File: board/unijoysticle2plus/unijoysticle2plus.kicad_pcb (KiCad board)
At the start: 4 copper layers, 62 x 49 mm, 43 parts, among them J1 DB9_Female, J2 DB9_Female, J3 USB_B_Micro, Q1 S8050, Q2 S8050, SW1 RESET, SW2 JOY SWAP, U1 74HC05, U2 74HC05, U3 74HC05, U4 ESP32-WROOM-32D, U5 AMS1117-3.3, U6 CH340C

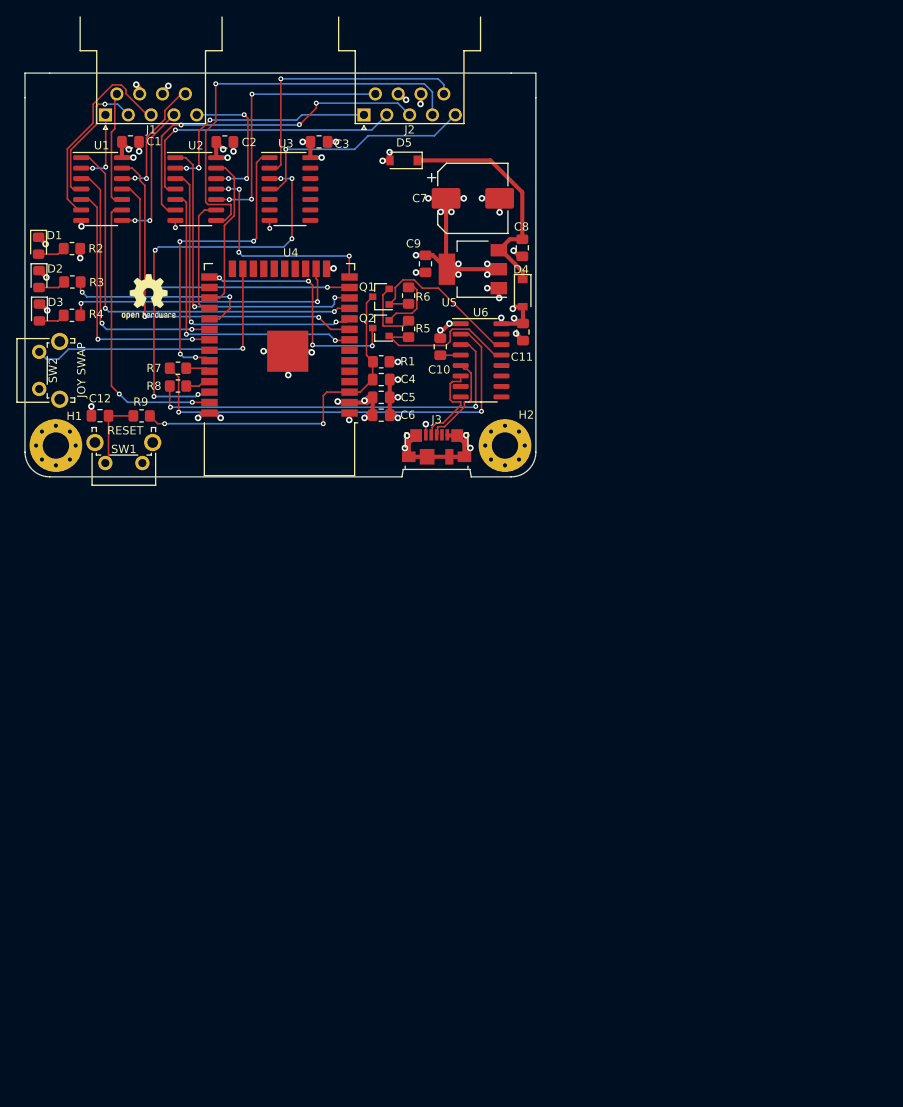
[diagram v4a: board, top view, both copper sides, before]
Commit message: unijoysticle2+: rev C WIP
- 5819 package: using SMA instead of SOD-123:
    - I thought the diode was fauly or something... so I dediced to
      change for another one. But I think the bug is somewhere else.
      In any case, using the new part (with different package)
- CH340C: powered using v3.3 instead of v5.
    - ESP EN should be high (v3.3) or low (0), but if CH340 is powered
      using v5, then DTR might have ~4V... instead of v3.3
- Using one MUN5214D insetad of two S8050 + resistors
    - less space, less routing, cheaper... although might not be as easy
      to solder as the S8050
- Using only one power place: removed VBUS and C64-5V power planes.
    - The only power plane is the v3.3+ one
- Layout changed a bit to based on the new components.
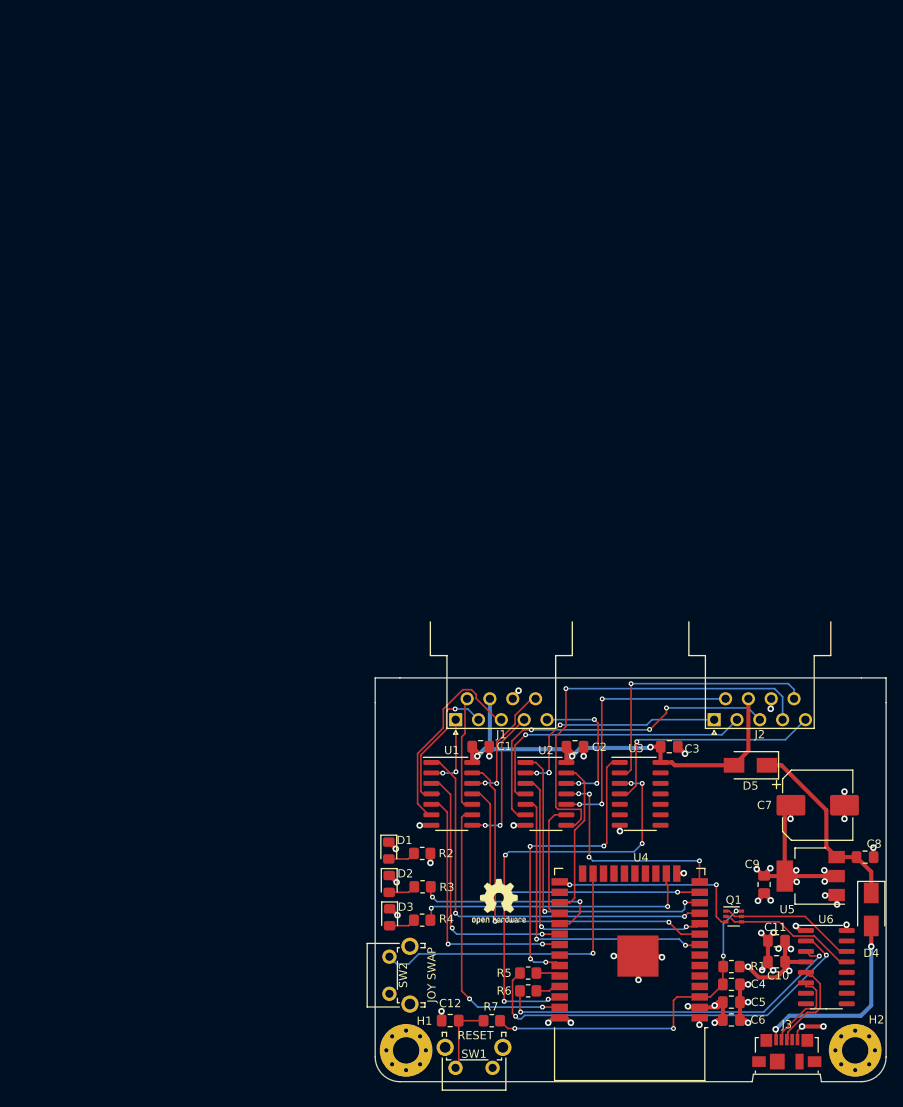
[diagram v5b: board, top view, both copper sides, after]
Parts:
- removed Q2: S8050, Package_TO_SOT_SMD:SOT-23
- removed the R5 at (86.8, 57.0)
- removed the R6 at (86.8, 52.9)
- C10: value .1uF -> 1uF
- D4, D5: footprint Diode_SMD:D_SOD-123 -> Diode_SMD:D_SMA
- Q1: value S8050 -> MUN5211DW1; footprint Package_TO_SOT_SMD:SOT-23 -> Package_TO_SOT_SMD:SOT-363_SC-70-6
- R2, R3, R4: value 300 -> 1k
- moved Q1 86.5 mm to (126.2, 128.3), turned to 0 degrees
- moved D4 85.9 mm to (142.9, 127.4)
- moved C9 85.8 mm to (129.9, 124.4)
- moved C10 85.1 mm to (131.4, 133.8), turned to 180 degrees
- moved C8 84.8 mm to (142.2, 121.1), turned to 0 degrees
- moved H2 84.8 mm to (141.0, 144.5)
- moved C1 84.8 mm to (95.5, 107.7)
- moved C2 84.8 mm to (107.0, 107.7)
- moved C3 84.8 mm to (118.4, 107.7)
- moved C4 84.8 mm to (126.0, 136.5)
- moved C6 84.8 mm to (126.0, 140.8)
- moved D1 84.8 mm to (84.4, 120.3)
- moved D2 84.8 mm to (84.4, 124.3)
- moved D3 84.8 mm to (84.5, 128.4)
- moved G*** 84.8 mm to (114.3, 119.8)
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- renumbered R7 to R5, R8 to R6, R9 to R7
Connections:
- C10 pad 1: Net-(C10-Pad1) -> +3V3
- C11 pad 1: VBUS -> +3V3
- J3 pad 6: GND -> Net-(J3-Pad6)
- Q1 pad 2: Net-(Q1-Pad2) -> /DTR_PROG
- Q1 pad 3: /ESP_EN -> /ESP_BOOT
- U6 pad 16: VBUS -> +3V3
- U6 pad 4: Net-(C10-Pad1) -> +3V3
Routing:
- net VDD: track 18.2 -> 60.0 mm, vias 10 -> 3
- net VBUS: track 9.34 -> 23.7 mm, vias 4 -> 2
- net GND: track 73.0 -> 59.9 mm, vias 35 -> 36
- net +3V3: track 43.6 -> 55.4 mm, vias 14 -> 16
- net Net-(Q1-Pad2): track 8.16 -> 0.00 mm
- net Net-(Q2-Pad2): track 7.35 -> 0.00 mm
- net Net-(C8-Pad1): track 28.4 -> 23.2 mm
- net /ESP_BOOT: track 29.6 -> 24.5 mm, vias 4 -> 2
- net Net-(R6-Pad2): track 48.5 -> 43.6 mm
- net /RTS_PROG: track 21.3 -> 16.7 mm
- net Net-(R5-Pad2): track 53.6 -> 50.1 mm
- net Net-(C10-Pad1): track 2.49 -> 0.00 mm
- net /DTR_PROG: track 19.4 -> 17.0 mm
- net /USBD-: track 11.3 -> 10.3 mm
- net /J2_POTY: track 28.6 -> 29.4 mm
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- removed copper zone on In2.Cu, net VBUS
- removed copper zone on In2.Cu, net VDD
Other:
- outline, holes or cut-outs redrawn

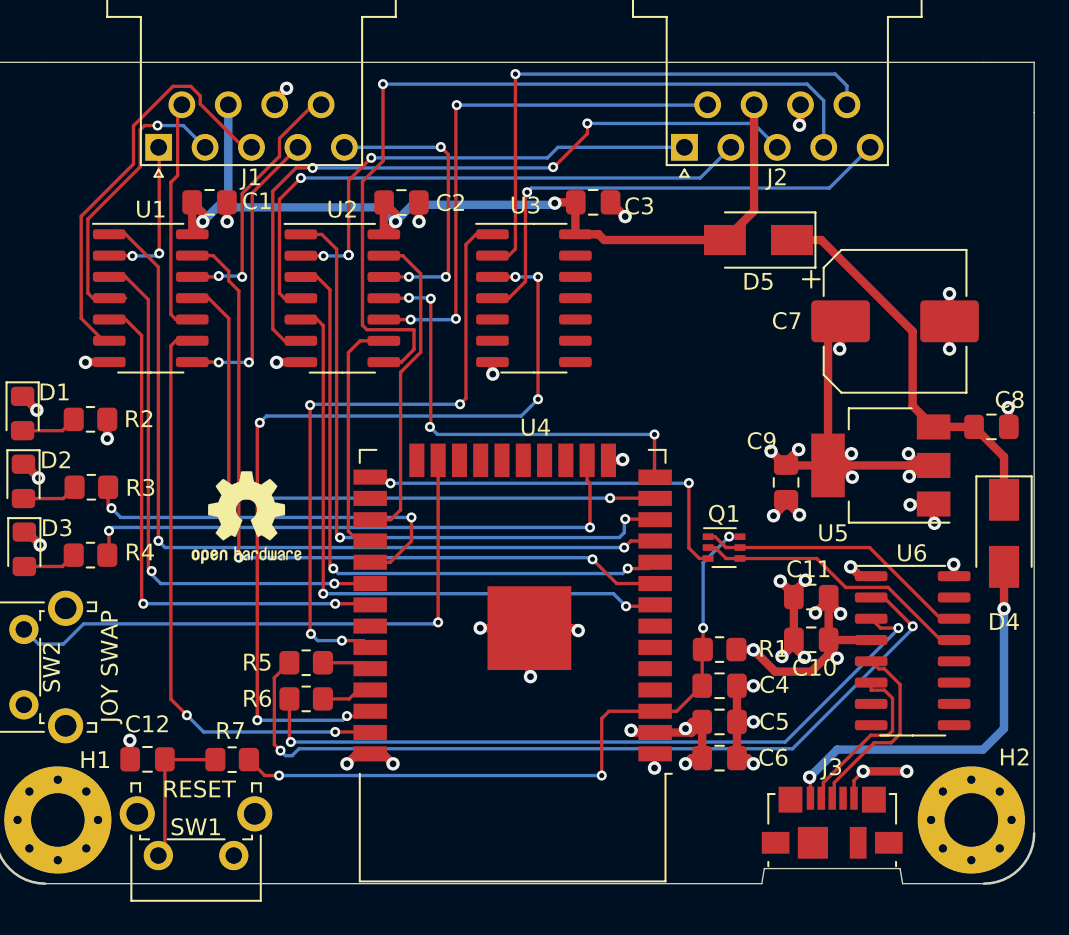
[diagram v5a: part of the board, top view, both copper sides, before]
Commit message: unijoysticle2plus: boot button and more
- Remove power plane. Plane #2 and #3 are GND planes now
- Add Boot button, easier to debug should we need it
- New USB Micro B package + footprint
- Renamed VDD with +5V
- Added PWR_FLAG for +5v to prevent warnings
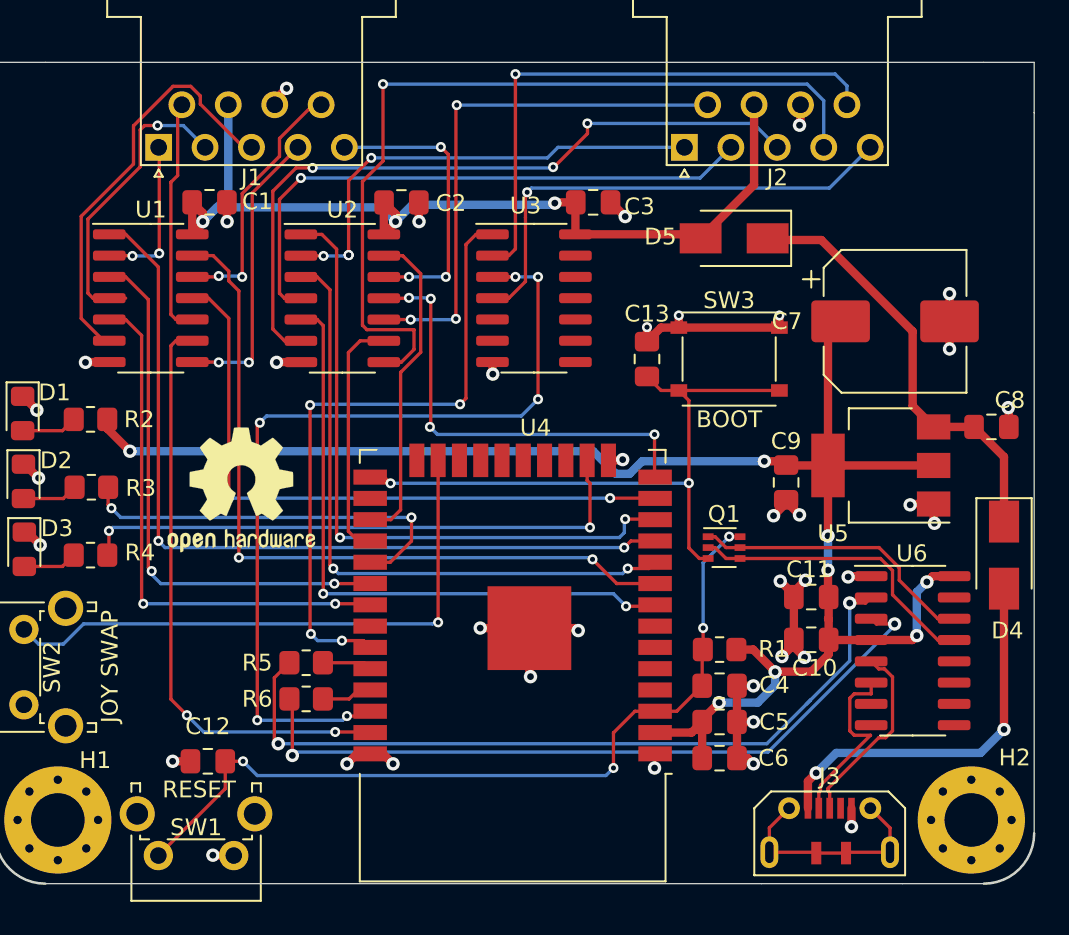
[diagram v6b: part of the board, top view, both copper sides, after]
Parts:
- removed R7: 0, Resistor_SMD:R_0805_2012Metric_Pad1.20x1.40mm_HandSolder
- removed the REF** at (97.7, 126.5)
- added C13: .1uF, Capacitor_SMD:C_0805_2012Metric_Pad1.18x1.45mm_HandSolder, F.Cu at (121.6, 117.0)
- added REF**: OSHW-Logo2_9.8x8mm_SilkScreen, Symbol:OSHW-Logo2_9.8x8mm_SilkScreen, F.Cu at (97.4, 124.8)
- added SW3: BOOT, Unijoysticle:SW_Push_1P1T_NO_5.1x5.1mm, F.Cu at (126.5, 117.0)
- J3: footprint Connector_USB:USB_Micro-B_Molex_47346-0001 -> Unijoysticle:MicroXNJ
- moved C12 3.60 mm to (95.4, 141.0)
- moved D5 1.45 mm to (126.8, 109.8)
- moved D4 1.30 mm to (142.9, 128.7)
- moved J3 0.88 mm to (132.5, 143.8), turned to 180 degrees
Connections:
- net VDD renamed +5V
- C12 pad 2: Net-(C12-Pad2) -> /ESP_EN
- SW1 pad 2: Net-(C12-Pad2) -> /ESP_EN
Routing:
- net +3V3: track 55.4 -> 101.2 mm, vias 16 -> 8
- net /ESP_BOOT: track 24.5 -> 38.5 mm
- net Net-(J3-Pad6): track 0.15 -> 13.5 mm
- net Net-(C12-Pad2): track 8.98 -> 0.00 mm
- net GND: track 59.9 -> 68.3 mm, vias 36 -> 39
- net /ESP_EN: track 41.9 -> 49.7 mm
- net Net-(C8-Pad1): track 23.2 -> 26.0 mm
- net Net-(R5-Pad2): track 50.1 -> 47.4 mm
- net +5V: track 60.0 -> 59.0 mm
- net /DTR_PROG: track 17.0 -> 17.8 mm
- net VBUS: track 23.7 -> 23.0 mm
- net /USBD-: track 10.3 -> 11.0 mm
- net Net-(R6-Pad2): track 43.6 -> 44.2 mm
- added copper zone on In2.Cu, net GND
- removed copper zone on In2.Cu, net +3V3
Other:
- outline, holes or cut-outs redrawn

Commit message: unijoysticle2plus: rev C
Rev C submitted to JLCPCB.
Added missing JLCPCB parts
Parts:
- R5, R6: value 1K -> 1k
- U4: value ESP32-WROOM-32D -> ESP32-WROOM-32E
